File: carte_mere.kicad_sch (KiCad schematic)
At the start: 53 parts, among them J10 Conn_01x02_Pin, J11 Conn_01x02_Pin, J12 Conn_01x02_Pin, J13 Conn_01x02_Pin, J14 Conn_01x02, J20 Conn_01x04, J23 Conn_01x02, J24 Conn_01x02

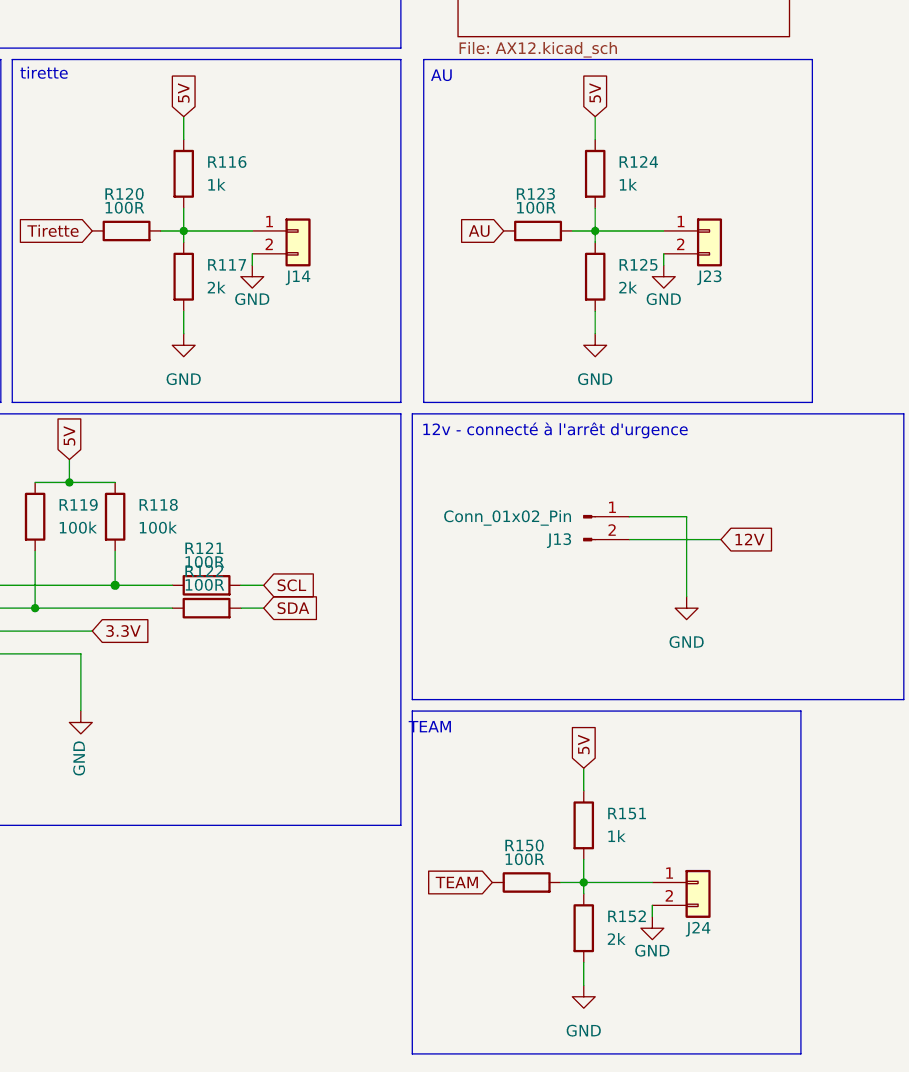
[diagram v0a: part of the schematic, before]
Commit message: fix issue on switch input
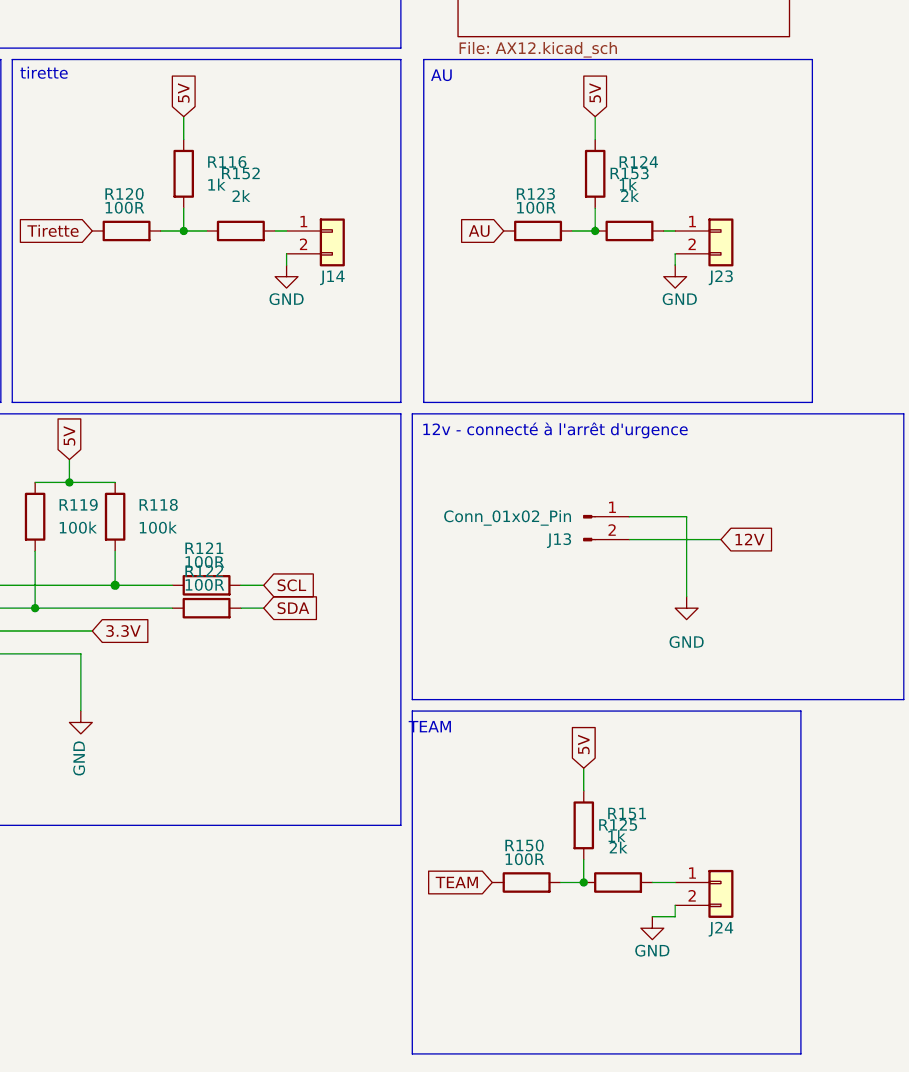
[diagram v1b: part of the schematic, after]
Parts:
- removed R117: 2k, Capacitor_SMD:C_0402_1005Metric, symbol Device:R
- added R153: 2k, Capacitor_SMD:C_0402_1005Metric, symbol Device:R
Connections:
- net GND: no longer R125.2, R152.2
- net at R123.2, R124.2: now also R153.1; no longer J23.1 (Pin_1), R125.1
- net at R116.2, R120.2: now also R152.1; no longer J14.1 (Pin_1)
- net at R150.2, R151.2: now also R125.1; no longer J24.1 (Pin_1), R152.1
- new net: J23.1 (Pin_1), R153.2
- new net: J14.1 (Pin_1), R152.2
- new net: J24.1 (Pin_1), R125.2
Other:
- moved on the sheet: J14, J23, J24

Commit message: fix issues
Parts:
- removed R153: 2k, Capacitor_SMD:C_0402_1005Metric, symbol Device:R
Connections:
- net 3.3V: now also R124.1
- net 5V: no longer R124.1
- net QEI_1_A: now also JP1.JP2_16 (D18); no longer JP1.JP2_15 (E17)
- net QEI_1_B: now also JP1.JP2_15 (E17); no longer JP1.JP2_28 (G18)
- net QEI_3_A: now also JP1.JP2_28 (G18); no longer JP1.JP2_16 (D18)
- net at J23.1 (Pin_1): now also R123.2, R124.2
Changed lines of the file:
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@@
 	)
 	(junction
-		(at 120.65 74.93)
+		(at 153.67 134.62)
 		(diameter 0)
 		(color 0 0 0 0)
 	)
 	(junction
-		(at 81.28 125.73)
+		(at 120.65 74.93)
 		(diameter 0)
 		(color 0 0 0 0)
 	)
 	(junction
-		(at 153.67 134.62)
+		(at 81.28 125.73)
 		(diameter 0)
 		(color 0 0 0 0)
@@
 	(wire
 		(pts
+			(xy 153.67 134.62) (xy 162.56 134.62)
+		)
+		(stroke
+			(width 0)
+			(type default)
+		)
+	)
+	(wire
+		(pts
 			(xy 233.68 81.28) (xy 236.22 81.28)
 		)
@@
 	(wire
 		(pts
-			(xy 162.56 134.62) (xy 161.29 134.62)
-		)
-		(stroke
-			(width 0)
-			(type default)
-		)
-	)
-	(wire
-		(pts
 			(xy 91.44 162.56) (xy 95.25 162.56)
 		)
@@
 		)
 	)
-	(global_label "5V"
+	(global_label "3.3V"
 		(shape input)
 		(at 153.67 121.92 90)
@@
 		)
 		(property "Intersheetrefs" "${INTERSHEET_REFS}"
-			(at 153.67 116.6367 90)
+			(at 153.67 114.8224 90)
 			(effects
 				(font
@@
 		)
 	)
+	(global_label "QEI_1_A"
+		(shape input)
+		(at 104.14 57.15 0)
+		(fields_autoplaced yes)
+		(effects
+			(font
+				(size 1.27 1.27)
+			)
+			(justify left)
+		)
+		(property "Intersheetrefs" "${INTERSHEET_REFS}"
+			(at 114.4428 57.15 0)
+			(effects
+				(font
+					(size 1.27 1.27)
+				)
+				(justify left)
+				(hide yes)
+			)
+		)
+	)
 	(global_label "AU"
 		(shape input)
@@
 		)
 	)
+	(global_label "QEI_1_B"
+		(shape input)
+		(at 80.01 57.15 180)
+		(fields_autoplaced yes)
+		(effects
+			(font
+				(size 1.27 1.27)
+			)
+			(justify right)
+		)
+		(property "Intersheetrefs" "${INTERSHEET_REFS}"
+			(at 69.5258 57.15 0)
+			(effects
+				(font
+					(size 1.27 1.27)
+				)
+				(justify right)
+				(hide yes)
+			)
+		)
+	)
 	(global_label "RX-lidar_1"
 		(shape input)
@@
 		)
 	)
-	(global_label "QEI_3_A"
-		(shape input)
-		(at 104.14 57.15 0)
-		(fields_autoplaced yes)
-		(effects
-			(font
-				(size 1.27 1.27)
-			)
-			(justify left)
-		)
-		(property "Intersheetrefs" "${INTERSHEET_REFS}"
-			(at 114.4428 57.15 0)
-			(effects
-				(font
-					(size 1.27 1.27)
-				)
-				(justify left)
-				(hide yes)
-			)
-		)
-	)
 	(global_label "5V"
 		(shape input)
@@
 		)
 	)
-	(global_label "QEI_1_A"
-		(shape input)
-		(at 80.01 57.15 180)
-		(fields_autoplaced yes)
-		(effects
-			(font
-				(size 1.27 1.27)
-			)
-			(justify right)
-		)
-		(property "Intersheetrefs" "${INTERSHEET_REFS}"
-			(at 69.7072 57.15 0)
-			(effects
-				(font
-					(size 1.27 1.27)
-				)
-				(justify right)
-				(hide yes)
-			)
-		)
-	)
 	(global_label "spare3_1"
 		(shape input)
@@
 		)
 	)
-	(global_label "QEI_1_B"
-		(shape input)
-		(at 121.92 72.39 0)
-		(fields_autoplaced yes)
-		(effects
-			(font
-				(size 1.27 1.27)
-			)
-			(justify left)
-		)
-		(property "Intersheetrefs" "${INTERSHEET_REFS}"
-			(at 132.4042 72.39 0)
-			(effects
-				(font
-					(size 1.27 1.27)
-				)
-				(justify left)
-				(hide yes)
-			)
-		)
-	)
 	(global_label "spare2_8"
 		(shape input)
@@
 		)
 	)
+	(global_label "QEI_3_A"
+		(shape input)
+		(at 121.92 72.39 0)
+		(fields_autoplaced yes)
+		(effects
+			(font
+				(size 1.27 1.27)
+			)
+			(justify left)
+		)
+		(property "Intersheetrefs" "${INTERSHEET_REFS}"
+			(at 132.2228 72.39 0)
+			(effects
+				(font
+					(size 1.27 1.27)
+				)
+				(justify left)
+				(hide yes)
+			)
+		)
+	)
 	(global_label "SERVO10"
 		(shape input)
@@
 					(unit 1)
 				)
-			)
-		)
-	)
-	(symbol
-		(lib_id "Device:R")
-		(at 157.48 134.62 90)
-		(unit 1)
-		(exclude_from_sim no)
-		(in_bom yes)
-		(on_board yes)
-		(dnp no)
-		(fields_autoplaced yes)
-		(property "Reference" "R153"
-			(at 157.48 128.27 90)
-			(effects
-				(font
-					(size 1.27 1.27)
-				)
-			)
-		)
-		(property "Value" "2k"
-			(at 157.48 130.81 90)
-			(effects
-				(font
-					(size 1.27 1.27)
-				)
-			)
-		)
-		(property "Footprint" "Capacitor_SMD:C_0402_1005Metric"
-			(at 157.48 136.398 90)
-			(effects
-				(font
-					(size 1.27 1.27)
-				)
-				(hide yes)
-			)
-		)
-		(property "Datasheet" "~"
-			(at 157.48 134.62 0)
-			(effects
-				(font
-					(size 1.27 1.27)
-				)
-				(hide yes)
-			)
-		)
-		(property "Description" "Resistor"
-			(at 157.48 134.62 0)
-			(effects
-				(font
-					(size 1.27 1.27)
-				)
-				(hide yes)
-			)
-		)
-		(pin "1"
-		)
-		(pin "2"
-		)
-		(instances
-			(project "carte_mere"
-				(path "/20c56496-71e7-4272-aa93-980e4fc2cc62"
-					(reference "R153")
-					(unit 1)
-				)

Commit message: test nouvelle forme de carte
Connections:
- net RX-lidar_2: now also JP1.JP2_4 (G15); no longer JP1.JP1_39 (T12)
- net SERVO1: now also JP1.JP2_2 (L17); no longer JP1.JP2_1 (L16)
- net SERVO10: now also JP1.JP1_39 (T12); no longer JP1.JP2_4 (G15)
- net SERVO2: now also JP1.JP2_1 (L16); no longer JP1.JP2_3 (H15)
- net SERVO9: now also JP1.JP1_40 (U12); no longer JP1.JP2_2 (L17)
- net TX-lidar_2: now also JP1.JP2_3 (H15); no longer JP1.JP1_40 (U12)
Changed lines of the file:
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@@
 	(wire
 		(pts
-			(xy 106.68 39.37) (xy 101.6 39.37)
+			(xy 107.95 39.37) (xy 101.6 39.37)
 		)
 		(stroke
@@
 		)
 	)
+	(global_label "TX-lidar_2"
+		(shape input)
+		(at 80.01 41.91 180)
+		(fields_autoplaced yes)
+		(effects
+			(font
+				(size 1.27 1.27)
+			)
+			(justify right)
+		)
+		(property "Intersheetrefs" "${INTERSHEET_REFS}"
+			(at 66.744 41.91 0)
+			(effects
+				(font
+					(size 1.27 1.27)
+				)
+				(justify right)
+				(hide yes)
+			)
+		)
+	)
 	(global_label "spare1_1"
 		(shape input)
@@
 		)
 	)
+	(global_label "SERVO1"
+		(shape input)
+		(at 107.95 39.37 0)
+		(fields_autoplaced yes)
+		(effects
+			(font
+				(size 1.27 1.27)
+			)
+			(justify left)
+		)
+		(property "Intersheetrefs" "${INTERSHEET_REFS}"
+			(at 118.1923 39.37 0)
+			(effects
+				(font
+					(size 1.27 1.27)
+				)
+				(justify left)
+				(hide yes)
+			)
+		)
+	)
 	(global_label "spare3_7"
 		(shape input)
@@
 		)
 	)
-	(global_label "SERVO1"
-		(shape input)
-		(at 80.01 39.37 180)
-		(fields_autoplaced yes)
-		(effects
-			(font
-				(size 1.27 1.27)
-			)
-			(justify right)
-		)
-		(property "Intersheetrefs" "${INTERSHEET_REFS}"
-			(at 69.7677 39.37 0)
-			(effects
-				(font
-					(size 1.27 1.27)
-				)
-				(justify right)
-				(hide yes)
-			)
-		)
-	)
 	(global_label "spare2_7"
 		(shape input)
@@
 		)
 	)
-	(global_label "SERVO9"
-		(shape input)
-		(at 106.68 39.37 0)
-		(fields_autoplaced yes)
-		(effects
-			(font
-				(size 1.27 1.27)
-			)
-			(justify left)
-		)
-		(property "Intersheetrefs" "${INTERSHEET_REFS}"
-			(at 116.9223 39.37 0)
-			(effects
-				(font
-					(size 1.27 1.27)
-				)
-				(justify left)
-				(hide yes)
-			)
-		)
-	)
 	(global_label "spare3_3"
 		(shape input)
@@
 		)
 	)
+	(global_label "SERVO9"
+		(shape input)
+		(at 58.42 87.63 0)
+		(fields_autoplaced yes)
+		(effects
+			(font
+				(size 1.27 1.27)
+			)
+			(justify left)
+		)
+		(property "Intersheetrefs" "${INTERSHEET_REFS}"
+			(at 68.6623 87.63 0)
+			(effects
+				(font
+					(size 1.27 1.27)
+				)
+				(justify left)
+				(hide yes)
+			)
+		)
+	)
 	(global_label "spare1_5"
 		(shape input)
@@
 		)
 	)
-	(global_label "RX-lidar_2"
+	(global_label "SERVO10"
 		(shape input)
 		(at 38.1 87.63 180)
@@
 		)
 		(property "Intersheetrefs" "${INTERSHEET_REFS}"
-			(at 24.5316 87.63 0)
+			(at 26.6482 87.63 0)
 			(effects
 				(font
@@
 		)
 	)
+	(global_label "RX-lidar_2"
+		(shape input)
+		(at 106.68 41.91 0)
+		(fields_autoplaced yes)
+		(effects
+			(font
+				(size 1.27 1.27)
+			)
+			(justify left)
+		)
+		(property "Intersheetrefs" "${INTERSHEET_REFS}"
+			(at 120.2484 41.91 0)
+			(effects
+				(font
+					(size 1.27 1.27)
+				)
+				(justify left)
+				(hide yes)
+			)
+		)
+	)
 	(global_label "spare1_3"
 		(shape input)
@@
 		)
 	)
-	(global_label "TX-lidar_2"
-		(shape input)
-		(at 58.42 87.63 0)
-		(fields_autoplaced yes)
-		(effects
-			(font
-				(size 1.27 1.27)
-			)
-			(justify left)
-		)
-		(property "Intersheetrefs" "${INTERSHEET_REFS}"
-			(at 71.686 87.63 0)
-			(effects
-				(font
-					(size 1.27 1.27)
-				)
-				(justify left)
-				(hide yes)
-			)
-		)
-	)
 	(global_label "spare1_8"
 		(shape input)
@@
 		)
 	)
-	(global_label "SERVO2"
-		(shape input)
-		(at 80.01 41.91 180)
-		(fields_autoplaced yes)
-		(effects
-			(font
-				(size 1.27 1.27)
-			)
-			(justify right)
-		)
-		(property "Intersheetrefs" "${INTERSHEET_REFS}"
-			(at 69.7677 41.91 0)
-			(effects
-				(font
-					(size 1.27 1.27)
-				)
-				(justify right)
-				(hide yes)
-			)
-		)
-	)
 	(global_label "SERVO13"
 		(shape input)
@@
 		)
 	)
+	(global_label "SERVO2"
+		(shape input)
+		(at 80.01 39.37 180)
+		(fields_autoplaced yes)
+		(effects
+			(font
+				(size 1.27 1.27)
+			)
+			(justify right)
+		)
+		(property "Intersheetrefs" "${INTERSHEET_REFS}"
+			(at 69.7677 39.37 0)
+			(effects
+				(font
+					(size 1.27 1.27)
+				)
+				(justify right)
+				(hide yes)
+			)
+		)
+	)
 	(global_label "spare2_8"
 		(shape input)
@@
 			(effects
 				(font
-					(size 1.27 1.27)
-				)
-				(justify left)
-				(hide yes)
-			)
-		)
-	)
-	(global_label "SERVO10"
-		(shape input)
-		(at 106.68 41.91 0)
-		(fields_autoplaced yes)
-		(effects
-			(font
-				(size 1.27 1.27)
-			)
-			(justify left)
-		)
-		(property "Intersheetrefs" "${INTERSHEET_REFS}"
-			(at 118.1318 41.91 0)
-			(effects
-				(font

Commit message: routage v2 ok - en attente de relecture
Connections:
- net AU: now also JP1.JP1_1 (N17); no longer JP1.JP2_40 (H20)
- net AX_DATA: now also JP1.JP2_32 (L20); no longer JP1.JP1_5 (T16)
- net AX_DIR: now also JP1.JP2_34 (F20); no longer JP1.JP1_7 (W18)
- net CAND: now also JP1.JP1_4 (R17); no longer JP1.JP1_1 (N17)
- net CANR: now also JP1.JP1_6 (U17); no longer JP1.JP1_2 (P18)
- net DSO_1: now also JP1.JP2_35 (M19); no longer JP1.JP2_7 (E18)
- net DSO_2: now also JP1.JP2_37 (K19); no longer JP1.JP2_8 (E19)
- net DSO_3: now also JP1.JP2_39 (J20); no longer JP1.JP2_9 (B19)
- net DSO_4: now also JP1.JP2_40 (H20); no longer JP1.JP2_14 (D20)
- net DSO_5: now also JP1.JP2_38 (J19); no longer JP1.JP2_13 (D19)
- net DSO_6: now also JP1.JP2_36 (M20); no longer JP1.JP2_10 (A20)
- net QEI_1_A: now also JP1.JP1_26 (T15); no longer JP1.JP2_16 (D18)
- net QEI_1_B: now also JP1.JP1_25 (T14); no longer JP1.JP2_15 (E17)
- net QEI_1_X: now also JP1.JP1_24 (W13); no longer JP1.JP2_18 (H17)
- net QEI_2_A: now also JP1.JP1_33 (P14); no longer JP1.JP2_24 (J16)
- net QEI_2_B: now also JP1.JP1_32 (W15); no longer JP1.JP2_25 (C20)
- net QEI_2_X: now also JP1.JP1_31 (V15); no longer JP1.JP2_26 (B20)
- net QEI_3_A: now also JP1.JP1_37 (U13); no longer JP1.JP2_28 (G18)
- net QEI_3_B: now also JP1.JP1_38 (V13); no longer JP1.JP2_23 (K16)
- net QEI_3_X: now also JP1.JP1_36 (U15); no longer JP1.JP2_22 (H18)
- net RX-lidar_1: now also JP1.JP1_5 (T16); no longer JP1.JP1_36 (U15)
- net RX-lidar_2: now also JP1.JP1_10 (Y19); no longer JP1.JP2_4 (G15)
- net RX-lidar_3: now also JP1.JP1_14 (Y17); no longer JP1.JP1_37 (U13)
- net SCL: now also JP1.JP1_21 (T17); no longer JP1.JP1_4 (R17)
- net SDA: now also JP1.JP1_20 (W16); no longer JP1.JP1_3 (R16)
- net SERVO11: now also JP1.JP1_35 (U14); no longer JP1.JP2_6 (F17)
- net SERVO12: now also JP1.JP1_34 (R14); no longer JP1.JP2_20 (G20)
- net SERVO13: now also JP1.JP1_27 (T11); no longer JP1.JP2_21 (J18)
- net SERVO14: now also JP1.JP1_28 (T10); no longer JP1.JP2_31 (L19)
- net SERVO15: now also JP1.JP1_23 (V12); no longer JP1.JP2_33 (F19)
- net SERVO16: now also JP1.JP1_22 (R18); no longer JP1.JP2_35 (M19)
- net SERVO3: now also JP1.JP2_4 (G15); no longer JP1.JP2_5 (F16)
- net SERVO4: now also JP1.JP2_3 (H15); no longer JP1.JP2_17 (H16)
- net SERVO5: now also JP1.JP2_5 (F16); no longer JP1.JP2_19 (G19)
- net SERVO6: now also JP1.JP2_6 (F17); no longer JP1.JP2_32 (L20)
- net SERVO7: now also JP1.JP2_26 (B20); no longer JP1.JP2_34 (F20)
- net SERVO8: now also JP1.JP2_27 (G17); no longer JP1.JP2_37 (K19)
- net TEAM: now also JP1.JP1_2 (P18); no longer JP1.JP2_39 (J20)
- net TX-lidar_1: now also JP1.JP1_8 (W19); no longer JP1.JP1_35 (U14)
- net TX-lidar_2: now also JP1.JP1_7 (W18); no longer JP1.JP2_3 (H15)
- net TX-lidar_3: now also JP1.JP1_9 (Y18); no longer JP1.JP1_38 (V13)
- net Tirette: now also JP1.JP1_3 (R16); no longer JP1.JP2_27 (G17)
- net spare1_1: now also JP1.JP1_19 (V16); no longer JP1.JP1_33 (P14)
- net spare1_2: now also JP1.JP1_18 (Y14); no longer JP1.JP1_34 (R14)
- net spare1_3: now also JP1.JP1_17 (W14); no longer JP1.JP1_31 (V15)
- net spare1_4: now also JP1.JP1_15 (V17); no longer JP1.JP1_26 (T15)
- net spare1_5: now also JP1.JP2_9 (B19); no longer JP1.JP1_32 (W15)
- net spare1_6: now also JP1.JP1_16 (V18); no longer JP1.JP1_25 (T14)
- net spare1_7: now also JP1.JP2_10 (A20); no longer JP1.JP1_27 (T11)
- net spare1_8: now also JP1.JP1_13 (Y16); no longer JP1.JP1_28 (T10)
- net spare2_1: now also JP1.JP2_18 (H17); no longer JP1.JP1_24 (W13)
- net spare2_2: now also JP1.JP2_16 (D18); no longer JP1.JP1_23 (V12)
- net spare2_3: now also JP1.JP2_17 (H16); no longer JP1.JP1_21 (T17)
- net spare2_4: now also JP1.JP2_15 (E17); no longer JP1.JP1_18 (Y14)
- net spare2_5: now also JP1.JP2_19 (G19); no longer JP1.JP1_22 (R18)
- net spare2_6: now also JP1.JP2_14 (D20); no longer JP1.JP1_17 (W14)
- net spare2_7: now also JP1.JP2_20 (G20); no longer JP1.JP1_19 (V16)
- net spare2_8: now also JP1.JP2_13 (D19); no longer JP1.JP1_20 (W16)
- net spare3_1: now also JP1.JP2_28 (G18); no longer JP1.JP1_14 (Y17)
- net spare3_2: now also JP1.JP2_24 (J16); no longer JP1.JP1_13 (Y16)
- net spare3_3: now also JP1.JP2_25 (C20); no longer JP1.JP1_9 (Y18)
- net spare3_4: now also JP1.JP2_23 (K16); no longer JP1.JP1_16 (V18)
- net spare3_5: now also JP1.JP2_31 (L19); no longer JP1.JP1_10 (Y19)
- net spare3_6: now also JP1.JP2_22 (H18); no longer JP1.JP1_15 (V17)
- net spare3_7: now also JP1.JP2_33 (F19); no longer JP1.JP1_8 (W19)
- net spare3_8: now also JP1.JP2_21 (J18); no longer JP1.JP1_6 (U17)

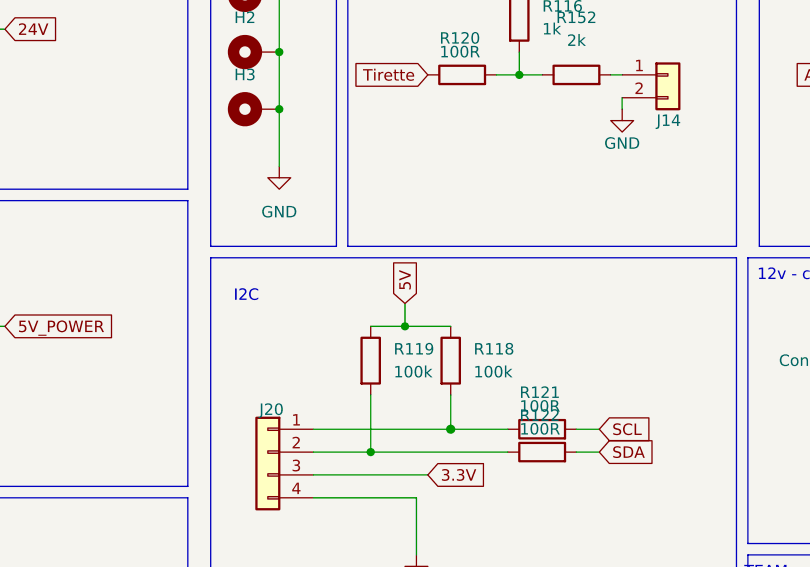
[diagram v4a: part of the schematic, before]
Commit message: fix issue on i2c
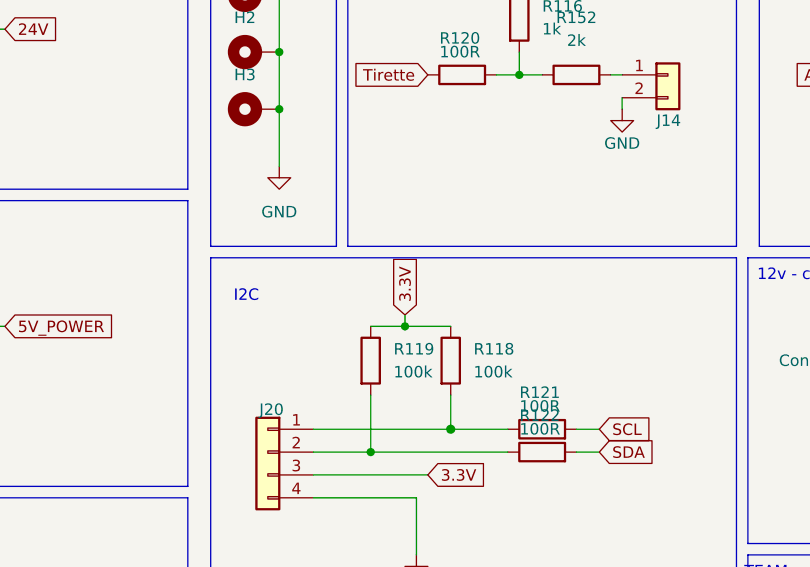
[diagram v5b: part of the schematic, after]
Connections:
- net 3.3V: now also R118.1, R119.1
- net 5V: no longer R118.1, R119.1
